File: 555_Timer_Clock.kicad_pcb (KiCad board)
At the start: 2 copper layers, 39 x 25 mm, 13 parts, among them J2 CLK_Out, U1 ICM7555xB

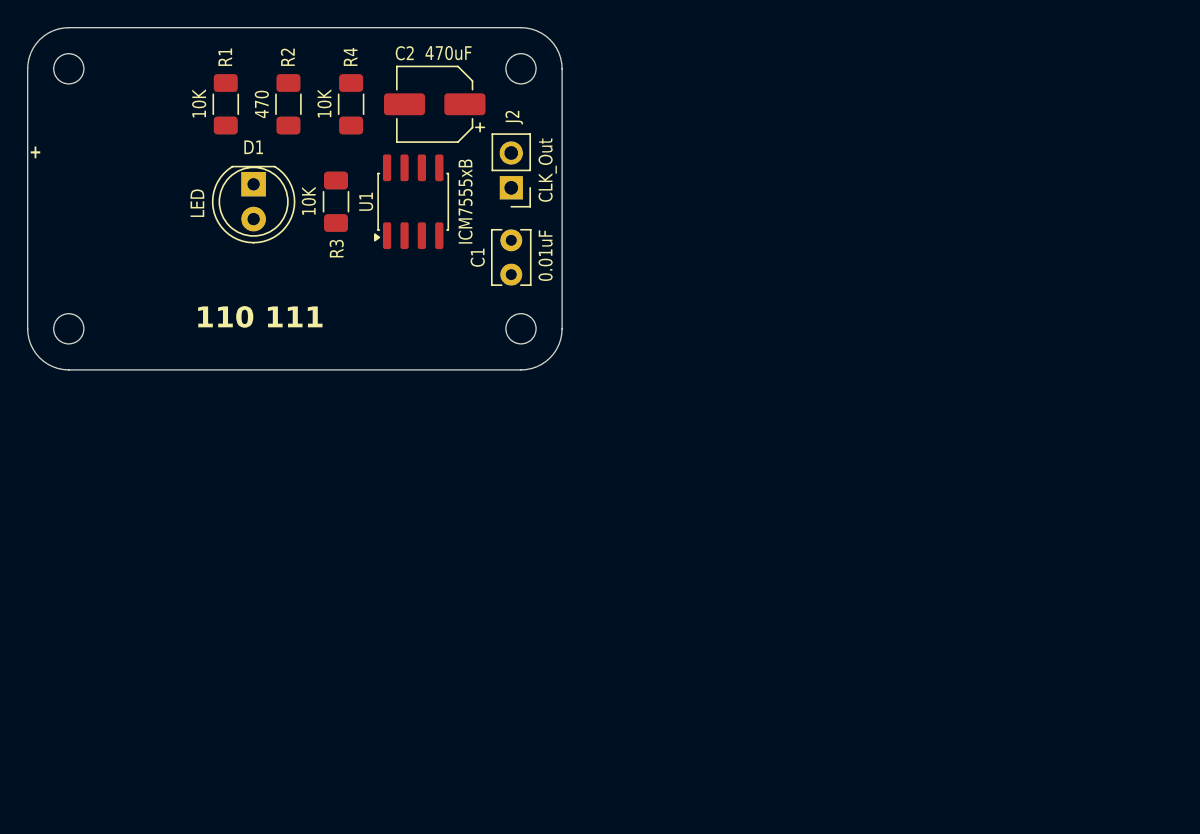
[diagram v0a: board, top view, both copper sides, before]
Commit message: Update PCB with connections
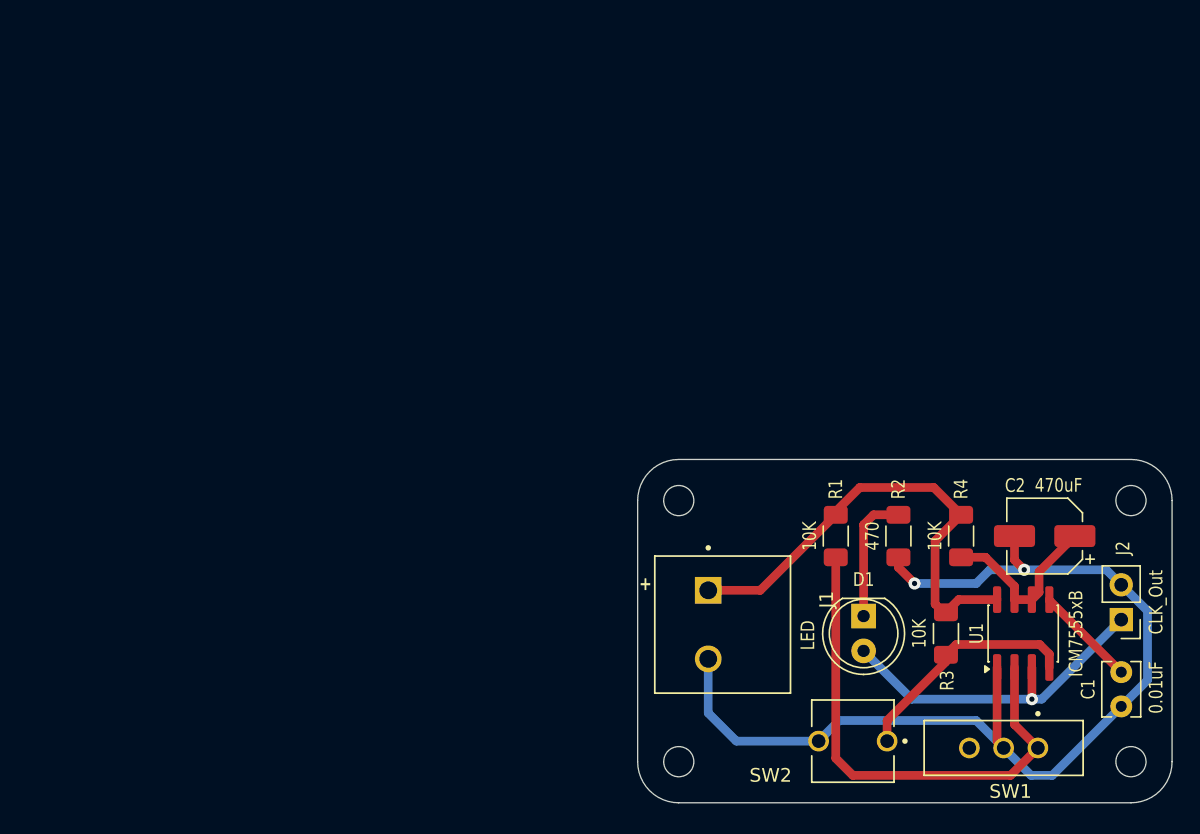
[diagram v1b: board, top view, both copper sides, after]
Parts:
- added J1: +5V, my_footprints:Terminal_Block_5mm, F.Cu at (146.4, 104.0)
- added SW1: Trigger, my_footprints:slide_switch_2.54mm, F.Cu at (168.0, 113.0)
- added SW2: RST, my_footprints:tact_switch_5mm, F.Cu at (157.0, 112.5)
- moved H4 54.6 mm to (177.3, 114.0)
- moved H2 54.6 mm to (144.3, 114.0)
- moved R1 54.5 mm to (155.8, 97.5)
- moved R2 54.5 mm to (160.3, 97.5)
- moved R3 54.5 mm to (163.8, 104.7)
- moved C1 54.5 mm to (176.6, 107.5)
- moved H3 54.5 mm to (177.3, 95.0)
- moved J2 54.5 mm to (176.6, 103.6)
- moved U1 54.5 mm to (169.4, 104.7)
- moved C2 54.5 mm to (171.0, 97.5)
- moved D1 54.5 mm to (157.8, 103.4)
- moved H1 54.5 mm to (144.3, 95.0)
- moved R4 54.5 mm to (164.9, 97.5)
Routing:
- net GND: track 0.00 -> 76.9 mm, vias 0 -> 2
- net /Trigger: track 0.00 -> 37.3 mm
- net /+5V: track 0.00 -> 35.0 mm, vias 0 -> 1
- net /CLK_Out: track 0.00 -> 25.1 mm, vias 0 -> 1
- net /RST: track 0.00 -> 17.2 mm
- net Net-(U1-DISCH): track 0.00 -> 12.9 mm
- net Net-(D1-K): track 0.00 -> 9.50 mm
- net Net-(U1-CONT): track 0.00 -> 7.46 mm
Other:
- board text removed: "110 111"

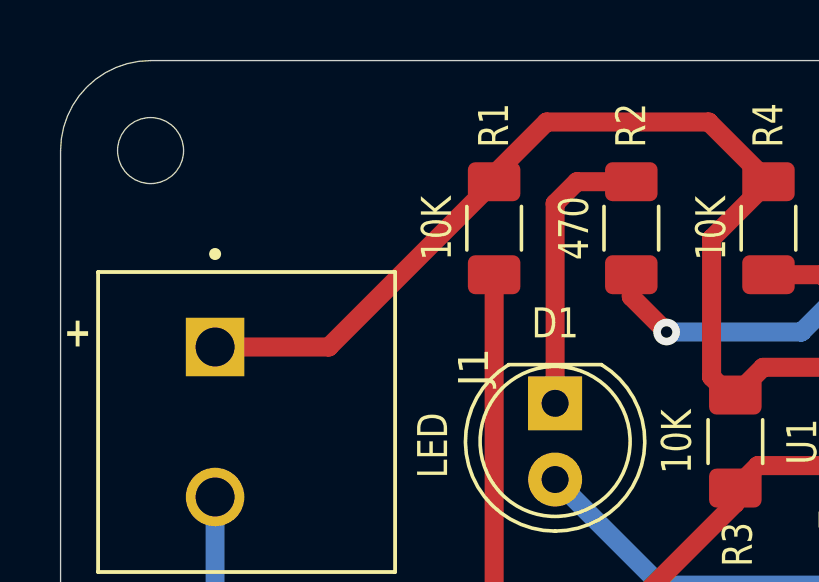
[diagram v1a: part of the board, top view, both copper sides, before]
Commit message: Add name to PCB
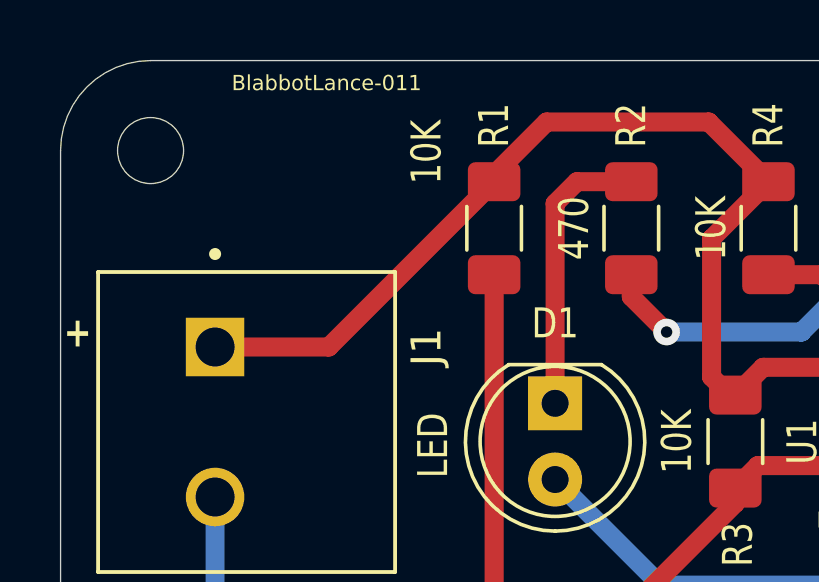
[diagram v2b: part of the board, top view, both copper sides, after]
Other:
- board text added: "BlabbotLance-011"
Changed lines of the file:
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@@
 		)
 		(property "Value" "10K"
-			(at 0 -1.905 90)
+			(at 2.54 -2.252 90)
 			(unlocked yes)
 			(layer "F.SilkS")
@@
 		(at 146.45 104 -90)
 		(property "Reference" "J1"
-			(at -1.825 -8.635 90)
+			(at -2.5 -7.05 90)
 			(layer "F.SilkS")
 			(effects
@@
 		(layer "Edge.Cuts")
 	)
+	(gr_text "BlabbotLance-011"
+		(at 147 93 0)
+		(layer "F.SilkS")
+		(effects
+			(font
+				(size 0.508 0.508)
+				(thickness 0.0508)
+			)
+			(justify left bottom)
+		)
+	)
 	(gr_text "+"

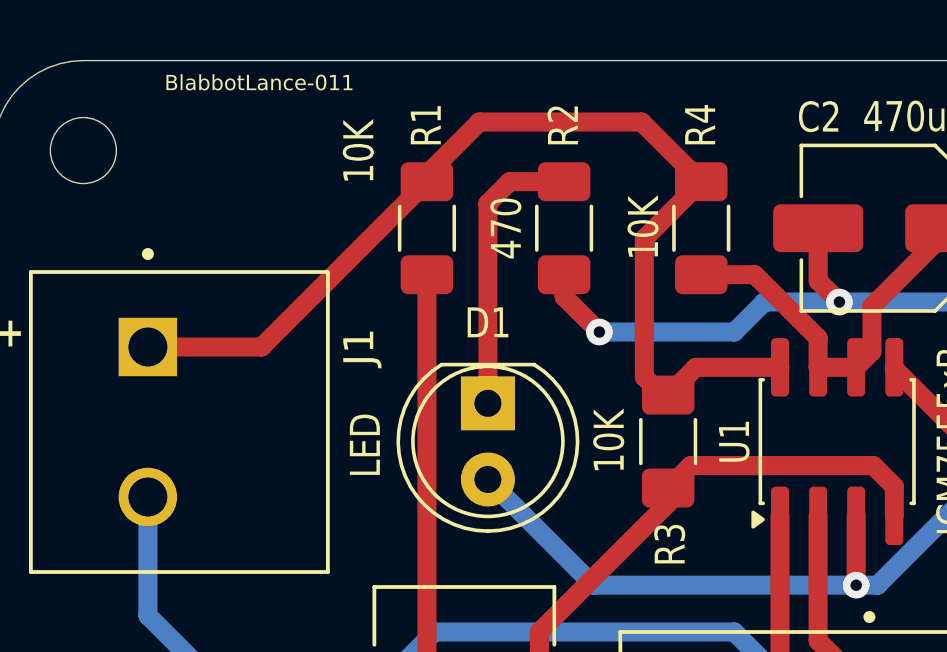
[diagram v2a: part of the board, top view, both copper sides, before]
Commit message: Add logo to PCB
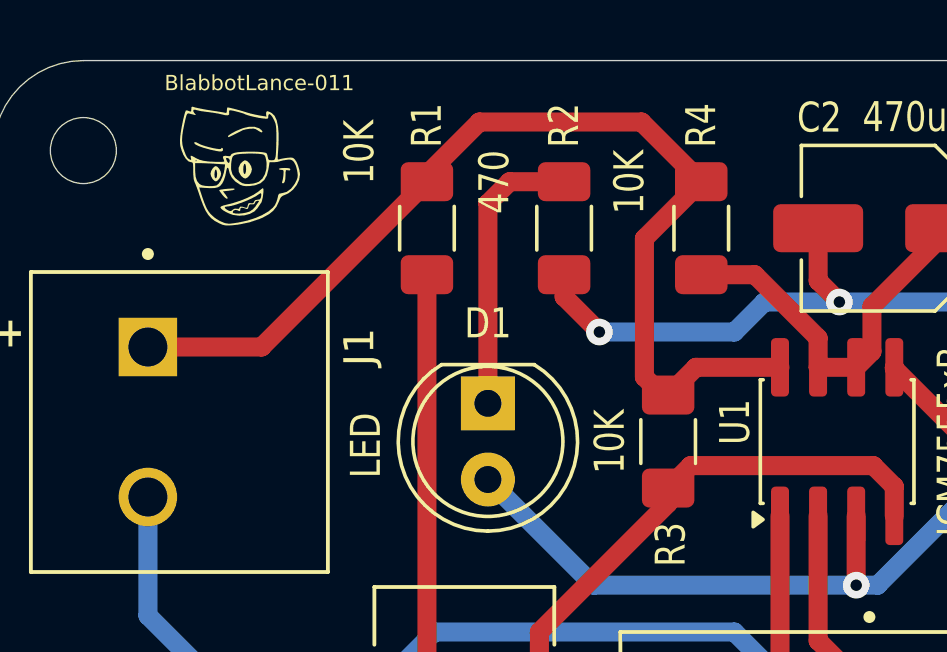
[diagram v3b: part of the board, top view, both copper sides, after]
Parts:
- added G***: LOGO, logo:lance_logo, F.Cu at (149.5, 95.5)
